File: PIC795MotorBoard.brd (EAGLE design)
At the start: 101.6 x 88.9 mm, 54 parts, among them J10 MOLEX-2P-156, J11 MOLEX_3P, J12 MOLEX_3P, J13 MOLEX_3P, J14 MOLEX_3P, J21 MOLEX_4PMOLEX_4P, J22 MOLEX_4PMOLEX_4P, J23 MOLEX_4PMOLEX_4P, J24 MOLEX_4PMOLEX_4P, J5 MOLEX_MINI_RA_3P, J6 MOLEX_MINI_RA_3P, J7 MOLEX_MINI_RA_3P, J8 MOLEX_MINI_RA_3P, U1 IFX9201SG, U2 IFX9201SG, U3 IFX9201SG, U4 IFX9201SG

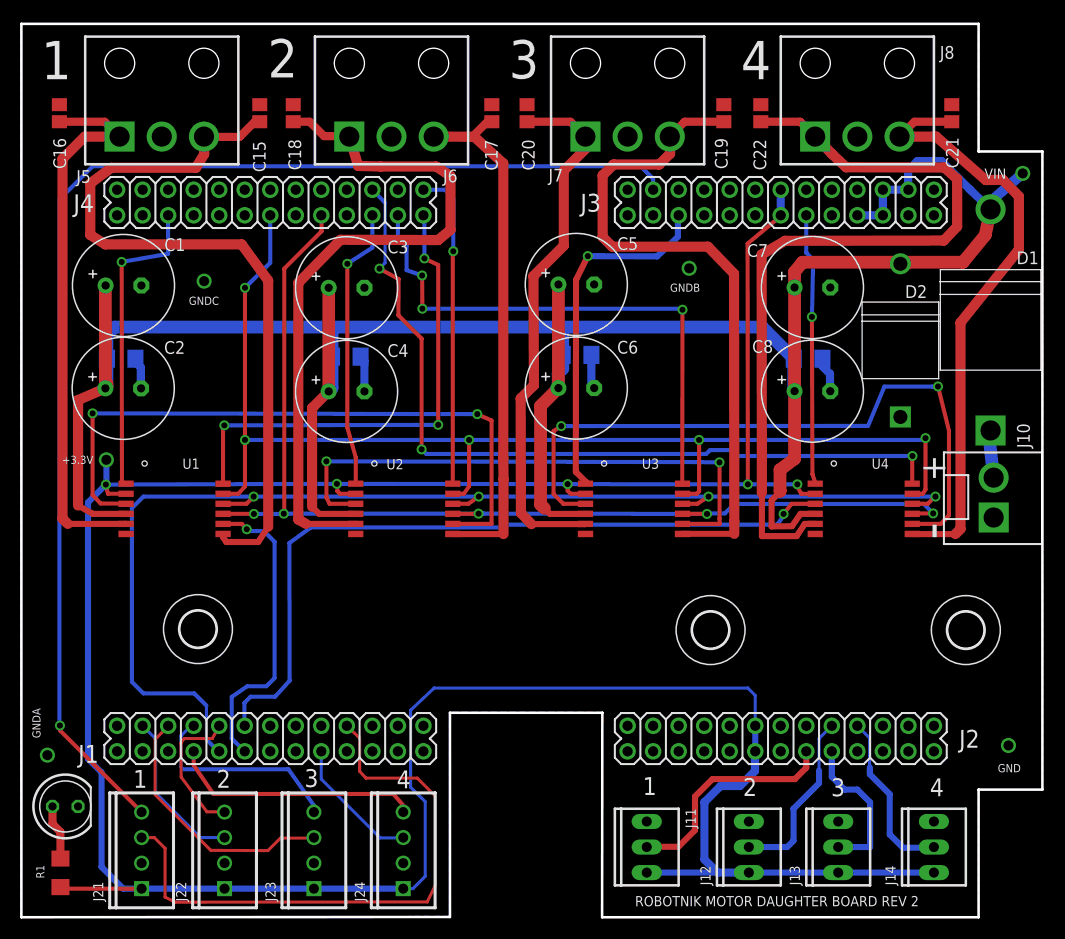
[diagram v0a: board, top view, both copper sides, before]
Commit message: Rev 2 board sent to PCB fab 8-11-19
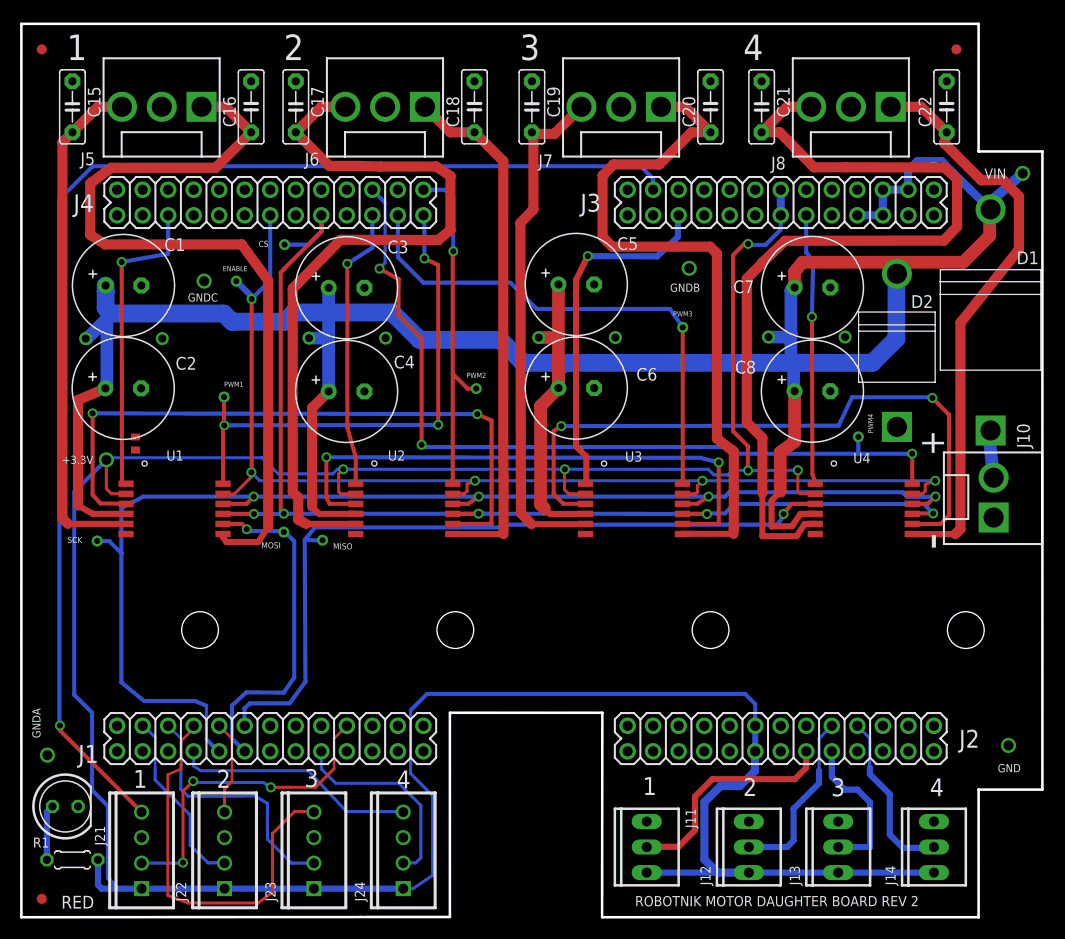
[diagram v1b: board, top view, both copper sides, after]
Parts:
- removed C13, C14: 0.1 uF, JimLib:1206
- removed H2, H4, H5: MOUNT-HOLE3.6, holes:3,6
- added C10, C9: 0.1 uF, JimLib:C0.3
- added CS, ENABLE, MISO, MOSI, PWM1, PWM2, PWM3, PWM4, SCK: TPTESTPAD-SMALL, JimLib:TESTPAD-SMALL
- added R2: 0 Ohm, JimLib:R0402
- added U$1, U$2, U$3: FIDUCIAL, adafruit:FIDUCIAL_1MM
- C11, C12: device JimLib:1206 -> JimLib:C0.3
- C15, C16, C17, C18, C19, C20, C21, C22: value 0.022 uF 200V -> 0.022 uF; device JimLib:C0805 -> JimLib:C5B2.5
- D2: value 38.9V -> TRANSZORB
- J5, J6, J7, J8: value MOLEX_MINI_RA_3P -> MOLEX_3PMOLEX-156-3P; device JimLib:MOLEX_MINI_RA_3P -> JimLib:MOLEX-156-3
- R1: value 330 ohms -> 220 ohms; device JimLib:R1206 -> JimLib:0204/5
- moved C12 45.9 mm to (78.2, 57.7)
- moved C11 45.4 mm to (55.3, 57.7)
- moved C17 19.5 mm to (27.3, 80.6), turned to 270 degrees
- moved C19 19.1 mm to (50.8, 80.6), turned to 270 degrees
- moved C16 19.1 mm to (22.9, 80.6), turned to 90 degrees
- moved C21 18.9 mm to (73.7, 80.6), turned to 270 degrees
- moved C15 18.7 mm to (5.08, 80.6), turned to 270 degrees
- moved C22 18.5 mm to (92.1, 80.6), turned to 90 degrees
- moved C20 18.3 mm to (68.6, 80.6), turned to 90 degrees
- moved C18 18.0 mm to (45.1, 80.6), turned to 90 degrees
- moved J7 5.75 mm to (59.7, 80.6)
- moved J8 5.75 mm to (82.5, 80.6)
- moved J6 5.75 mm to (36.2, 80.6)
- moved J5 5.71 mm to (14.0, 80.6)
- moved R1 1.76 mm to (5.08, 5.71), turned to 0 degrees
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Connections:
- net !SPI_CS: now also CS.P$1
- net DISABLE: now also ENABLE.P$1
- net ENC1: now also J21.2; no longer J21.3
- net ENC2: now also J22.2; no longer J22.3
- net ENC3: now also J23.2; no longer J23.3
- net ENC4: now also J24.2; no longer J24.3
- net GND: now also C10.2, C11.2, C12.2, C15.1, C16.2, C17.1, C18.2, C19.1, C20.2, C21.1, C22.2, C9.2, J21.3, J22.3, J23.3, J24.3, R2.1, R2.2; no longer C11.C, C12.C, C13.C, C14.C, C15.2, C16.1, C17.2, C18.1, C19.2, C20.1, C21.2, C22.1, J21.2, J22.2, J23.2, J24.2
- net N$10: now also C17.2, J6.3; no longer C18.2, J6.1
- net N$11: now also C20.1, J7.1; no longer C19.1, J7.3
- net N$12: now also C19.2, J7.3; no longer C20.2, J7.1
- net N$13: now also C22.1, J8.1; no longer C21.1, J8.3
- net N$14: now also C21.2, J8.3; no longer C22.2, J8.1
- net N$7: now also C16.1, J5.1; no longer C15.1, J5.3
- net N$8: now also C15.2, J5.3; no longer C16.2, J5.1
- net N$9: now also C18.1, J6.1; no longer C17.1, J6.3
- net OC2: now also PWM1.P$1
- net OC3: now also PWM2.P$1
- net OC4: now also PWM3.P$1
- net OC5: now also PWM4.P$1
- net SPI_MISO: now also MISO.P$1
- net SPI_MOSI: now also MOSI.P$1
- net SPI_SCK: now also SCK.P$1
- net VCC: now also C10.1, C11.1, C12.1, C9.1; no longer C11.A, C12.A, C13.A, C14.A
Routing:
- net ENC1: track 58.2 -> 32.5 mm, vias 0 -> 3
- net T3CK: track 20.6 -> 40.1 mm
- net VCC: track 255.8 -> 269.9 mm
- net GND: track 13.8 -> 0.00 mm
- net +3V3: track 299.9 -> 309.0 mm
- net DISABLE: track 118.5 -> 110.6 mm
- net ENC4: track 13.4 -> 20.3 mm
- net N$14: track 81.0 -> 87.3 mm
- net !SPI_CS: track 110.9 -> 117.0 mm
- net SPI_SCK: track 122.8 -> 127.8 mm
- net T5CK: track 14.2 -> 9.42 mm
- net N$10: track 70.8 -> 75.6 mm
- net N$8: track 55.5 -> 51.4 mm
- net SPI_MOSI: track 30.4 -> 34.1 mm
- net N$7: track 75.9 -> 79.3 mm
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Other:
- board text added: "RED"
